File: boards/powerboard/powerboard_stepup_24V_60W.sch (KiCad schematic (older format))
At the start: 2 parts

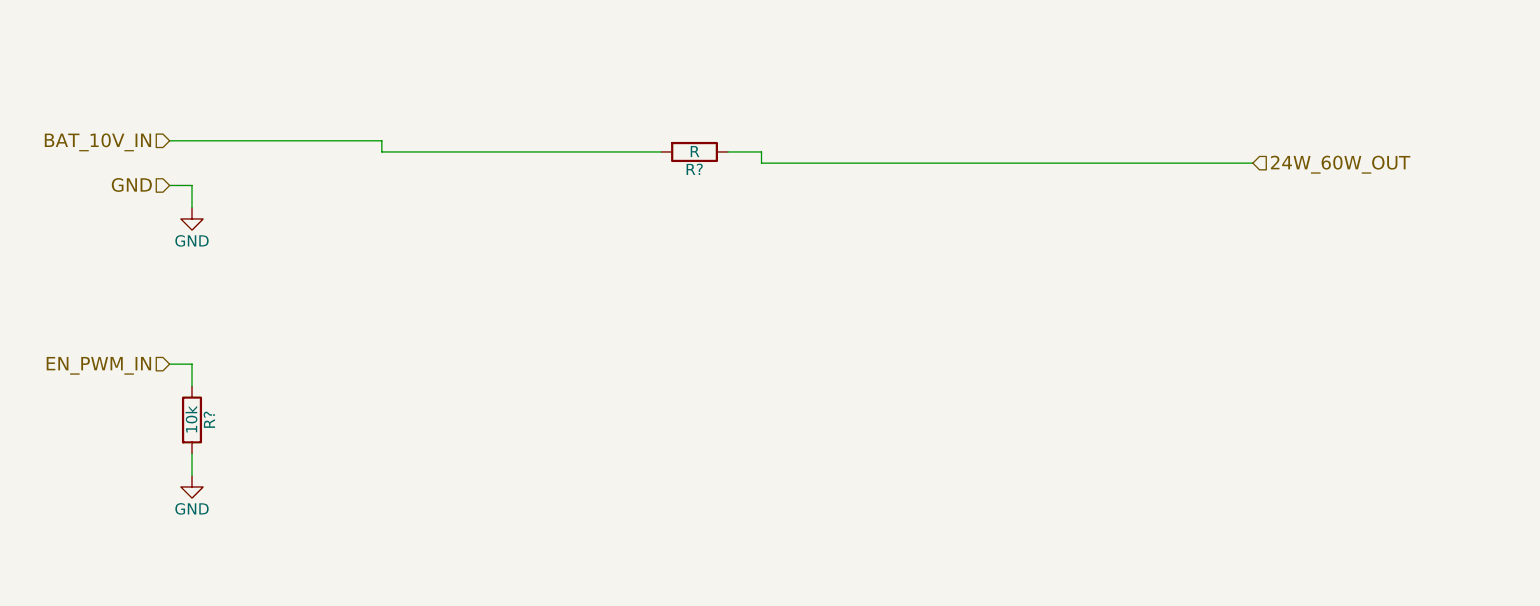
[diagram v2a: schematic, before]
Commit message: powerboard: add lt1370 boost converter
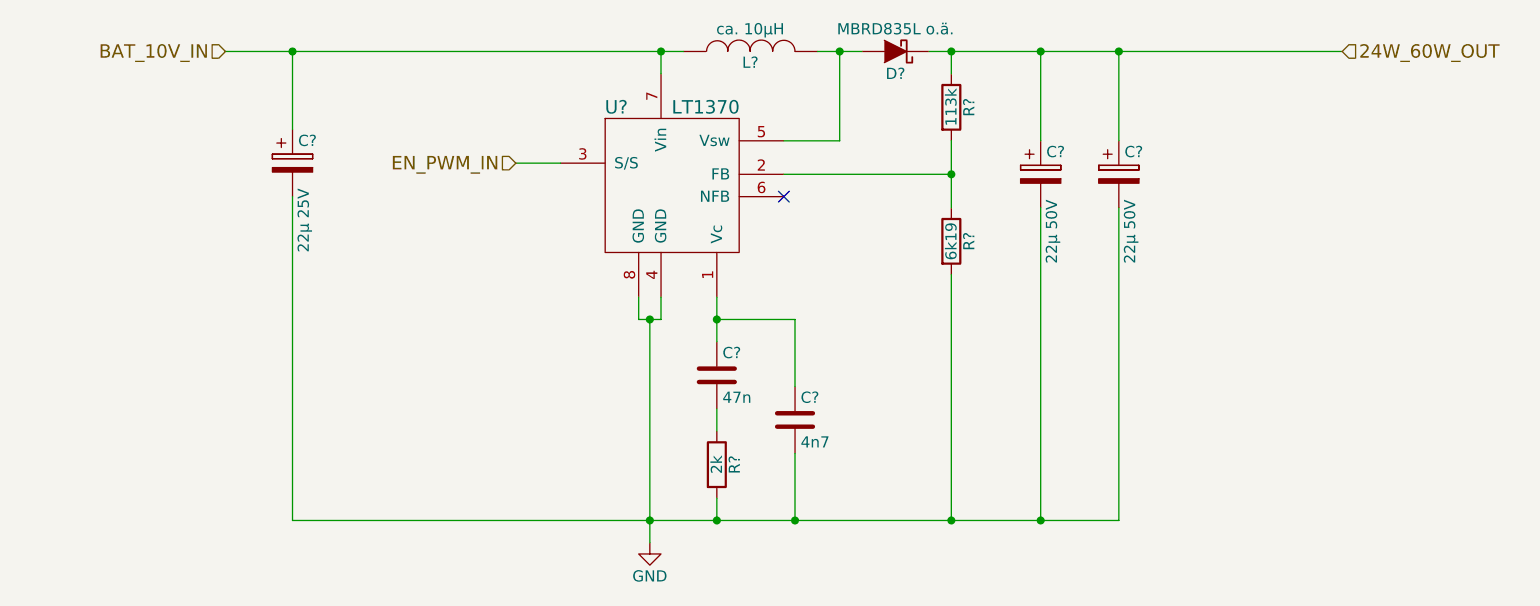
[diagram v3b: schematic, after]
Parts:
- removed R?: R, symbol R
- removed R?: 10k, symbol R
- added C?: 47n, symbol C
- added C?: 4n7, symbol C
- added C?: 22µ 25V, symbol CP
- added C? (x2): 22µ 50V, symbol CP
- added D?: MBRD835L o.ä., symbol D_Schottky
- added L?: ca. 10µH, symbol INDUCTOR
- added R?: 113k, symbol R
- added R?: 6k19, symbol R
- added R?: 2k, symbol R
- added U?: LT1370, symbol LT1370
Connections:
- net 24W_60W_OUT: now also C?.1, C?.1, D?.1 (K), R?.1
- net BAT_10V_IN: now also C?.1, L?.1, U?.7 (Vin)
- net EN_PWM_IN: now also U?.3 (S/S)
- net GND: now also C?.2, C?.2, C?.2, C?.2, R?.2, R?.2, U?.4 (GND), U?.8 (GND)
- new net: C?.1, C?.1, U?.1 (Vc)
- new net: R?.1, R?.2, U?.2 (FB)
- new net: D?.2 (A), L?.2, U?.5 (Vsw)
- new net: C?.2, R?.1
- no-connect marks 0 -> 1
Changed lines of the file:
@@
 LIBS:DRV8816
 LIBS:ACS711
+LIBS:lt1370
 LIBS:powerboard-cache
 EELAYER 25 0
@@
 Comment4 ""
 $EndDescr
-Text HLabel 1850 1850 0    60   Input ~ 0
+Text HLabel 2100 1450 0    60   Input ~ 0
 BAT_10V_IN
-Text HLabel 1850 2050 0    60   Input ~ 0
-GND
-$Comp
-L GND #PWR019
-U 1 1 58870495
-P 1950 2150
-AR Path="/5886F238/58870495" Ref="#PWR019"  Part="1"
-AR Path="/5886F2AA/58870495" Ref="#PWR021"  Part="1"
-AR Path="/5886F5A0/58870495" Ref="#PWR023"  Part="1"
-F 0 "#PWR023" H 1950 1900 50  0001 C CNN
-F 1 "GND" H 1950 2000 50  0000 C CNN
-F 2 "" H 1950 2150 50  0000 C CNN
-F 3 "" H 1950 2150 50  0000 C CNN
-	1    1950 2150
-	1    0    0    -1
-$EndComp
-Wire Wire Line
-	1850 2050 1950 2050
-Wire Wire Line
-	1950 2050 1950 2150
-Text HLabel 6700 1950 2    60   Input ~ 0
+Text HLabel 7100 1450 2    60   Input ~ 0
 24W_60W_OUT
-$Comp
-L R R?
-U 1 1 588704AE
-P 4200 1900
-AR Path="/5886F238/588704AE" Ref="R?"  Part="1"
-AR Path="/5886F2AA/588704AE" Ref="R?"  Part="1"
-AR Path="/5886F5A0/588704AE" Ref="R?"  Part="1"
-F 0 "R?" V 4280 1900 50  0000 C CNN
-F 1 "R" V 4200 1900 50  0000 C CNN
-F 2 "" V 4130 1900 50  0000 C CNN
-F 3 "" H 4200 1900 50  0000 C CNN
-	1    4200 1900
-	0    1    1    0
-$EndComp
-Wire Wire Line
-	6700 1950 4500 1950
-Wire Wire Line
-	4500 1950 4500 1900
-Wire Wire Line
-	4500 1900 4350 1900
-Wire Wire Line
-	4050 1900 2800 1900
-Wire Wire Line
-	2800 1900 2800 1850
-Wire Wire Line
-	2800 1850 1850 1850
-Text HLabel 1850 2850 0    60   Input ~ 0
+Text HLabel 3400 1950 0    60   Input ~ 0
 EN_PWM_IN
-$Comp
-L R R?
-U 1 1 58878248
-P 1950 3100
-AR Path="/5886F238/58878248" Ref="R?"  Part="1"
-AR Path="/5886F2AA/58878248" Ref="R?"  Part="1"
-AR Path="/5886F5A0/58878248" Ref="R?"  Part="1"
-F 0 "R?" V 2030 3100 50  0000 C CNN
-F 1 "10k" V 1950 3100 50  0000 C CNN
-F 2 "" V 1880 3100 50  0000 C CNN
-F 3 "" H 1950 3100 50  0000 C CNN
-	1    1950 3100
-	1    0    0    -1
-$EndComp
 $Comp
 L GND #PWR020
 U 1 1 58878312
-P 1950 3350
+P 4000 3650
 AR Path="/5886F238/58878312" Ref="#PWR020"  Part="1"
 AR Path="/5886F2AA/58878312" Ref="#PWR022"  Part="1"
 AR Path="/5886F5A0/58878312" Ref="#PWR024"  Part="1"
-F 0 "#PWR024" H 1950 3100 50  0001 C CNN
-F 1 "GND" H 1950 3200 50  0000 C CNN
-F 2 "" H 1950 3350 50  0000 C CNN
-F 3 "" H 1950 3350 50  0000 C CNN
-	1    1950 3350
-	1    0    0    -1
-$EndComp
-Wire Wire Line
-	1950 3350 1950 3250
-Wire Wire Line
-	1950 2950 1950 2850
-Wire Wire Line
-	1950 2850 1850 2850
+F 0 "#PWR020" H 4000 3400 50  0001 C CNN
+F 1 "GND" H 4000 3500 50  0000 C CNN
+F 2 "" H 4000 3650 50  0000 C CNN
+F 3 "" H 4000 3650 50  0000 C CNN
+	1    4000 3650
+	1    0    0    -1
+$EndComp
+$Comp
+L LT1370 U?
+U 1 1 588A8663
+P 4100 2050
+F 0 "U?" H 3850 2400 60  0000 C CNN
+F 1 "LT1370" H 4250 2400 60  0000 C CNN
+F 2 "" H 4950 1625 60  0000 C CNN
+F 3 "" H 4950 1625 60  0000 C CNN
+	1    4100 2050
+	1    0    0    -1
+$EndComp
+$Comp
+L INDUCTOR L?
+U 1 1 588A86BB
+P 4450 1450
+F 0 "L?" V 4400 1450 50  0000 C CNN
+F 1 "ca. 10µH" V 4550 1450 50  0000 C CNN
+F 2 "" H 4450 1450 50  0000 C CNN
+F 3 "" H 4450 1450 50  0000 C CNN
+	1    4450 1450
+	0    -1   -1   0
+$EndComp
+$Comp
+L D_Schottky D?
+U 1 1 588A86F2
+P 5100 1450
+F 0 "D?" H 5100 1550 50  0000 C CNN
+F 1 "MBRD835L o.ä." H 5100 1350 50  0000 C CNN
+F 2 "" H 5100 1450 50  0000 C CNN
+F 3 "" H 5100 1450 50  0000 C CNN
+	1    5100 1450
+	-1   0    0    1
+$EndComp
+Wire Wire Line
+	4600 1850 4850 1850
+Wire Wire Line
+	4850 1850 4850 1450
+Wire Wire Line
+	4750 1450 4950 1450
+Connection ~ 4850 1450
+Wire Wire Line
+	4050 1550 4050 1450
+Wire Wire Line
+	2100 1450 4150 1450
+$Comp
+L R R?
+U 1 1 588A8805
+P 5350 1700
+F 0 "R?" V 5430 1700 50  0000 C CNN
+F 1 "113k" V 5350 1700 50  0000 C CNN
+F 2 "" V 5280 1700 50  0000 C CNN
+F 3 "" H 5350 1700 50  0000 C CNN
+	1    5350 1700
+	1    0    0    -1
+$EndComp
+$Comp
+L R R?
+U 1 1 588A8867
+P 5350 2300
+F 0 "R?" V 5430 2300 50  0000 C CNN
+F 1 "6k19" V 5350 2300 50  0000 C CNN
+F 2 "" V 5280 2300 50  0000 C CNN
+F 3 "" H 5350 2300 50  0000 C CNN
+	1    5350 2300
+	1    0    0    -1
+$EndComp
+Wire Wire Line
+	5350 2150 5350 1850
+Wire Wire Line
+	4600 2000 5350 2000
+Connection ~ 5350 2000
+Wire Wire Line
+	5350 1550 5350 1450
+Wire Wire Line
+	5250 1450 7100 1450
+NoConn ~ 4600 2100
+$Comp
+L C C?
+U 1 1 588A8A56
+P 4300 2900
+F 0 "C?" H 4325 3000 50  0000 L CNN
+F 1 "47n" H 4325 2800 50  0000 L CNN
+F 2 "" H 4338 2750 50  0000 C CNN
+F 3 "" H 4300 2900 50  0000 C CNN
+	1    4300 2900
+	1    0    0    -1
+$EndComp
+$Comp
+L R R?
+U 1 1 588A8B43
+P 4300 3300
+F 0 "R?" V 4380 3300 50  0000 C CNN
+F 1 "2k" V 4300 3300 50  0000 C CNN
+F 2 "" V 4230 3300 50  0000 C CNN
+F 3 "" H 4300 3300 50  0000 C CNN
+	1    4300 3300
+	1    0    0    -1
+$EndComp
+$Comp
+L C C?
+U 1 1 588A8BB9
+P 4650 3100
+F 0 "C?" H 4675 3200 50  0000 L CNN
+F 1 "4n7" H 4675 3000 50  0000 L CNN
+F 2 "" H 4688 2950 50  0000 C CNN
+F 3 "" H 4650 3100 50  0000 C CNN
+	1    4650 3100
+	1    0    0    -1
+$EndComp
+Wire Wire Line
+	4300 2550 4300 2750
+Wire Wire Line
+	4300 2650 4650 2650
+Wire Wire Line
+	4650 2650 4650 2950
+Connection ~ 4300 2650
+Wire Wire Line
+	4300 3150 4300 3050
+Wire Wire Line
+	4000 2650 4000 3650
+Wire Wire Line
+	2400 3550 6100 3550
+Wire Wire Line
+	4300 3550 4300 3450
+Wire Wire Line
+	4650 3550 4650 3250
+Connection ~ 4300 3550
+Wire Wire Line
+	3950 2650 4050 2650
+Wire Wire Line
+	3950 2650 3950 2550
+Connection ~ 4000 3550
+Wire Wire Line
+	4050 2650 4050 2550
+Connection ~ 4000 2650
+Wire Wire Line
+	5350 3550 5350 2450
+Connection ~ 4650 3550
+Connection ~ 4050 1450
+Wire Wire Line
+	3400 1950 3600 1950
+$Comp
+L CP C?
+U 1 1 588A9B10
+P 2400 1950
+F 0 "C?" H 2425 2050 50  0000 L CNN
+F 1 "22µ 25V" V 2450 1550 50  0000 L CNN
+F 2 "" H 2438 1800 50  0000 C CNN
+F 3 "" H 2400 1950 50  0000 C CNN
+	1    2400 1950
+	1    0    0    -1
+$EndComp
+Wire Wire Line
+	2400 1800 2400 1450
+Connection ~ 2400 1450
+Wire Wire Line
+	2400 2100 2400 3550
+$Comp
+L CP C?
+U 1 1 588A9E5D
+P 5750 2000
+F 0 "C?" H 5775 2100 50  0000 L CNN
+F 1 "22µ 50V" V 5800 1600 50  0000 L CNN
+F 2 "" H 5788 1850 50  0000 C CNN
+F 3 "" H 5750 2000 50  0000 C CNN
+	1    5750 2000
+	1    0    0    -1
+$EndComp
+$Comp
+L CP C?
+U 1 1 588AA272
+P 6100 2000
+F 0 "C?" H 6125 2100 50  0000 L CNN
+F 1 "22µ 50V" V 6150 1600 50  0000 L CNN
+F 2 "" H 6138 1850 50  0000 C CNN
+F 3 "" H 6100 2000 50  0000 C CNN
+	1    6100 2000
+	1    0    0    -1
+$EndComp
+Wire Wire Line
+	5750 1450 5750 1850
+Connection ~ 5350 1450
+Wire Wire Line
+	6100 1450 6100 1850
+Connection ~ 5750 1450
+Connection ~ 6100 1450
+Wire Wire Line
+	5750 3550 5750 2150
+Connection ~ 5350 3550
+Wire Wire Line
+	6100 3550 6100 2150
+Connection ~ 5750 3550
 $EndSCHEMATC
